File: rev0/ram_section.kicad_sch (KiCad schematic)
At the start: 4 parts, among them IC1 ECP5-BGA256, U10 HyperRAM

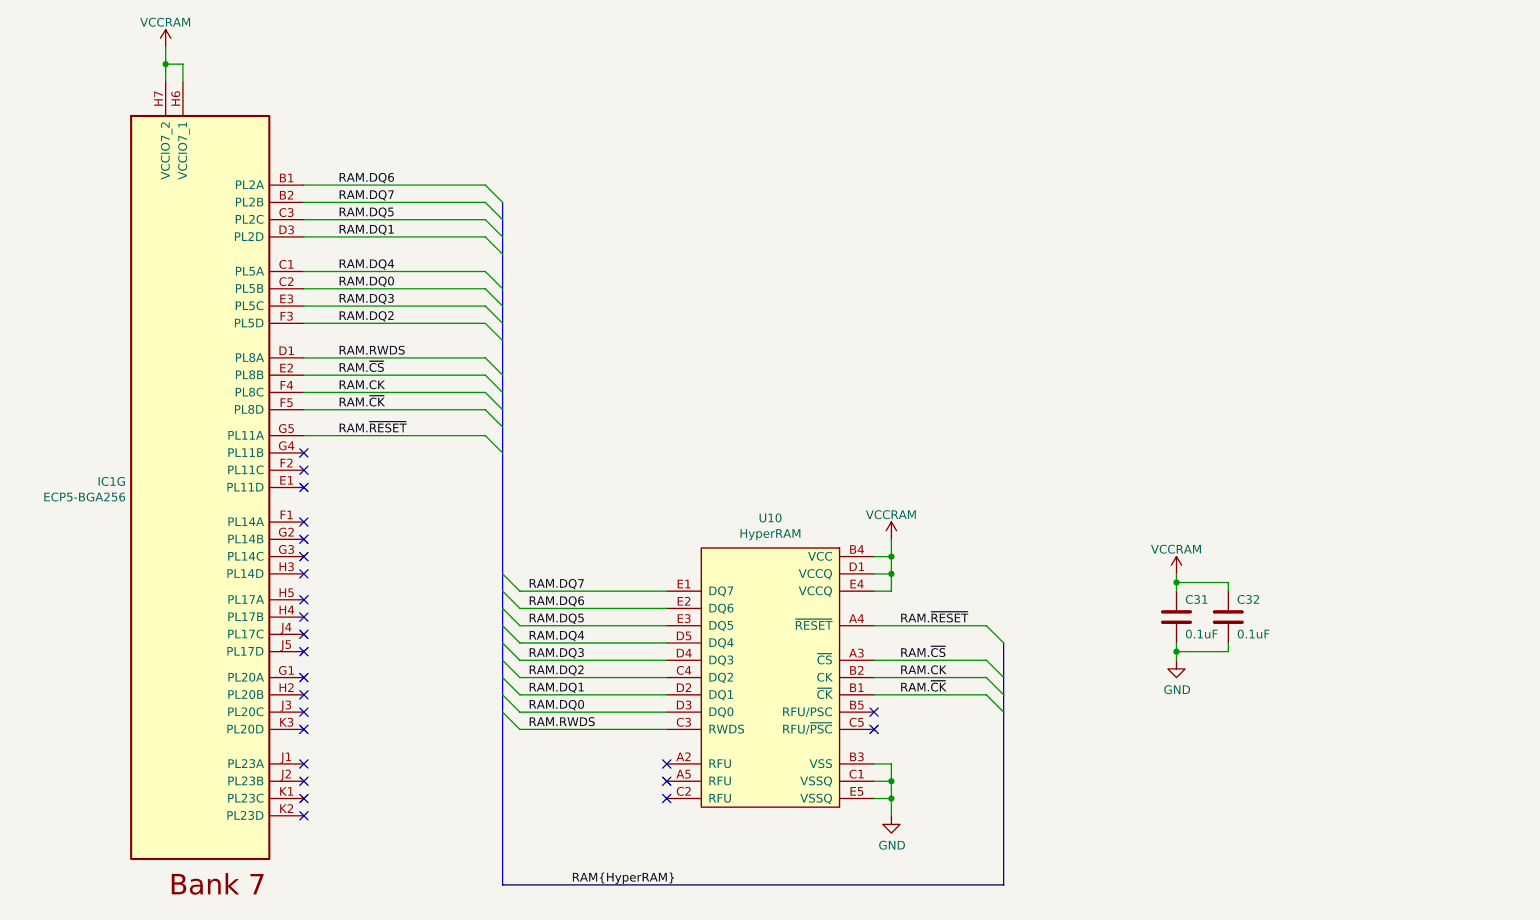
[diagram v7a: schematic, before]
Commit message: hardware: update layout to match schematic
- invert USB switch D+/D- for routing convenience
- connect *_VBUS_CLAMPED to *_VBUS_IN not *_VBUS
- reassign FPGA pins and banks for routing convenience
- connect PHY VBAT to +3V3, not +5V
- add PHY VDD33 test points
- add LED test points
- add PROGRAM button test point
- add PHY VDD33 test point
- add mezzanine connector
- improve decoupling
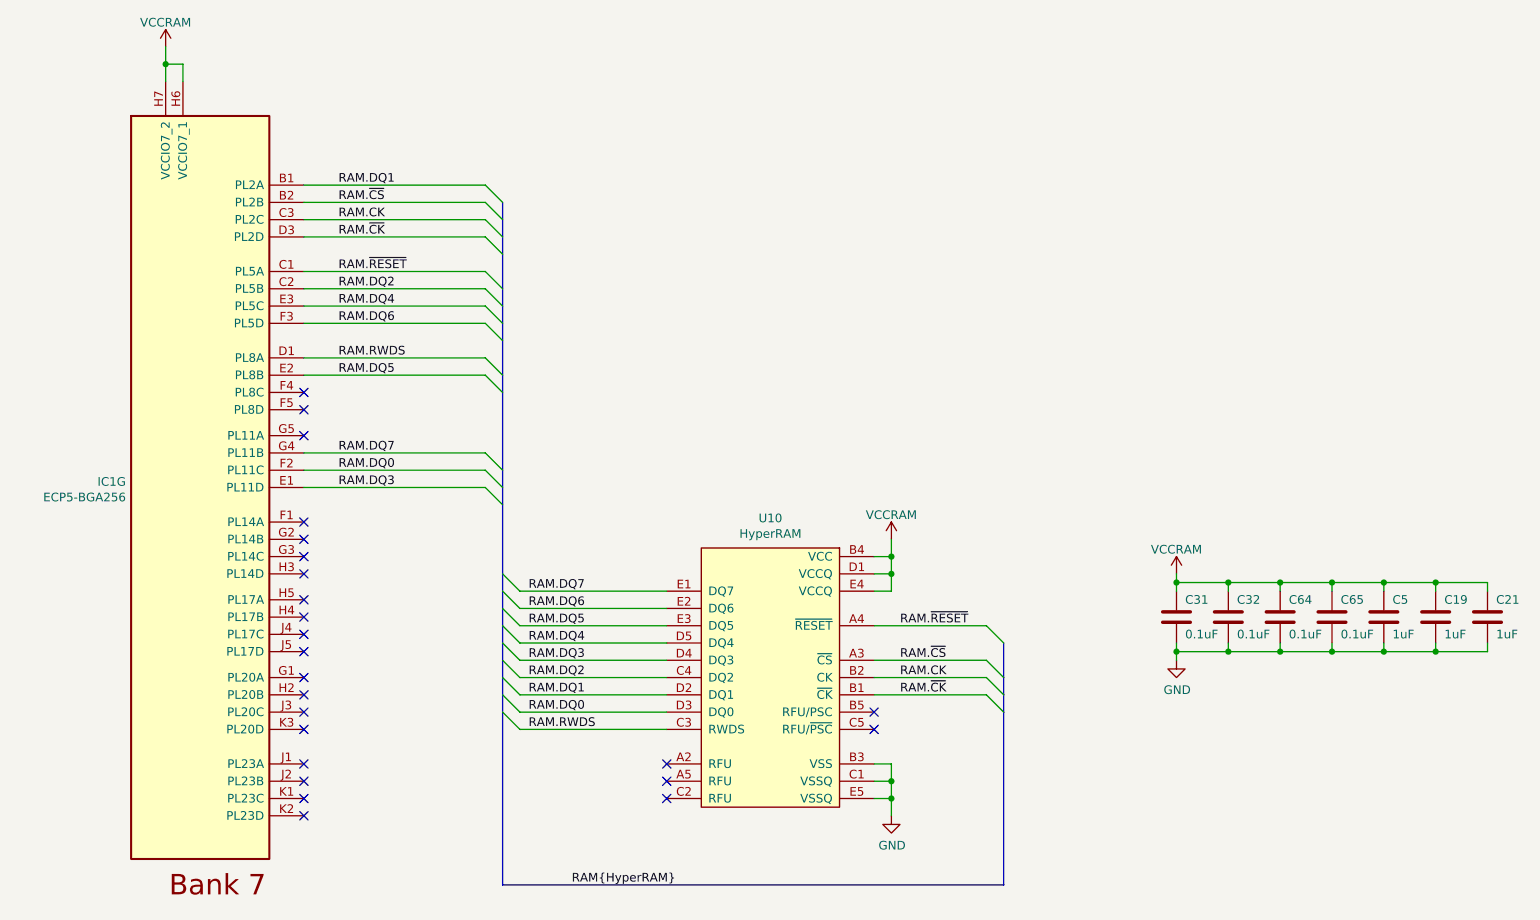
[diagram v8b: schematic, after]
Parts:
- added C19, C21, C5: 1uF, Capacitor_SMD:C_0402_1005Metric, symbol Device:C
- added C64, C65: 0.1uF, Capacitor_SMD:C_0402_1005Metric, symbol Device:C
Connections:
- net GND: now also C19.2, C21.2, C5.2, C64.2, C65.2
- net RAM.CK: now also IC1.C3 (PL2C); no longer IC1.F4 (PL8C)
- net RAM.DQ0: now also IC1.F2 (PL11C); no longer IC1.C2 (PL5B)
- net RAM.DQ1: now also IC1.B1 (PL2A); no longer IC1.D3 (PL2D)
- net RAM.DQ2: now also IC1.C2 (PL5B); no longer IC1.F3 (PL5D)
- net RAM.DQ3: now also IC1.E1 (PL11D); no longer IC1.E3 (PL5C)
- net RAM.DQ4: now also IC1.E3 (PL5C); no longer IC1.C1 (PL5A)
- net RAM.DQ5: now also IC1.E2 (PL8B); no longer IC1.C3 (PL2C)
- net RAM.DQ6: now also IC1.F3 (PL5D); no longer IC1.B1 (PL2A)
- net RAM.DQ7: now also IC1.G4 (PL11B); no longer IC1.B2 (PL2B)
- net RAM.~{CK}: now also IC1.D3 (PL2D); no longer IC1.F5 (PL8D)
- net RAM.~{CS}: now also IC1.B2 (PL2B); no longer IC1.E2 (PL8B)
- net RAM.~{RESET}: now also IC1.C1 (PL5A); no longer IC1.G5 (PL11A)
- net VCCRAM: now also C19.1, C21.1, C5.1, C64.1, C65.1
